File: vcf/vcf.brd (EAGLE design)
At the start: 88.9 x 107.6 mm, 102 parts, among them IC1 OPA4130U, IC2 OPA4130U, IC3 OPA4130U, IC4 OPA4130U, IC5 OPA4130U, Q1 BC847ASMD, Q2 BC847ASMD, Q3 BC847ASMD, Q4 BC847ASMD, Q5 BC847ASMD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

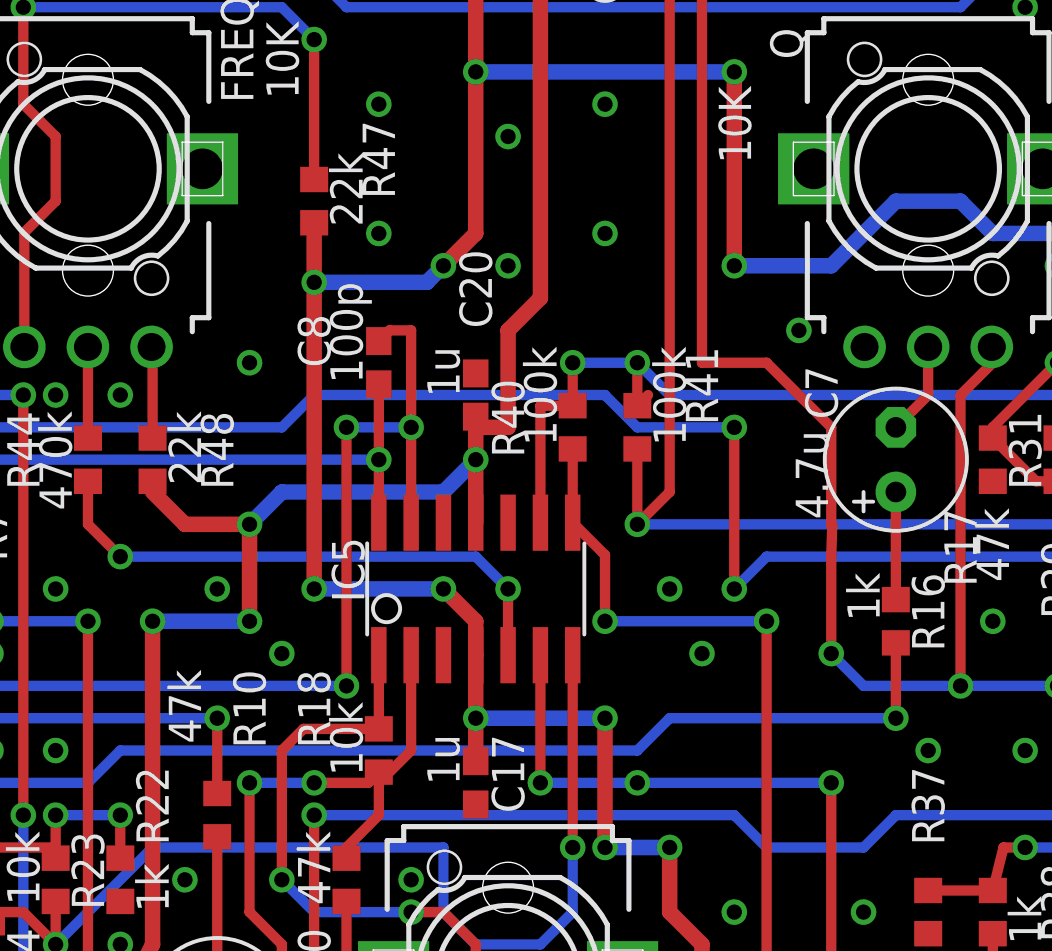
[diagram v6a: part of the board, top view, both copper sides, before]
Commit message: fixed bugs in vca.  did more changing of vcf components.  need to route a trace in vcf
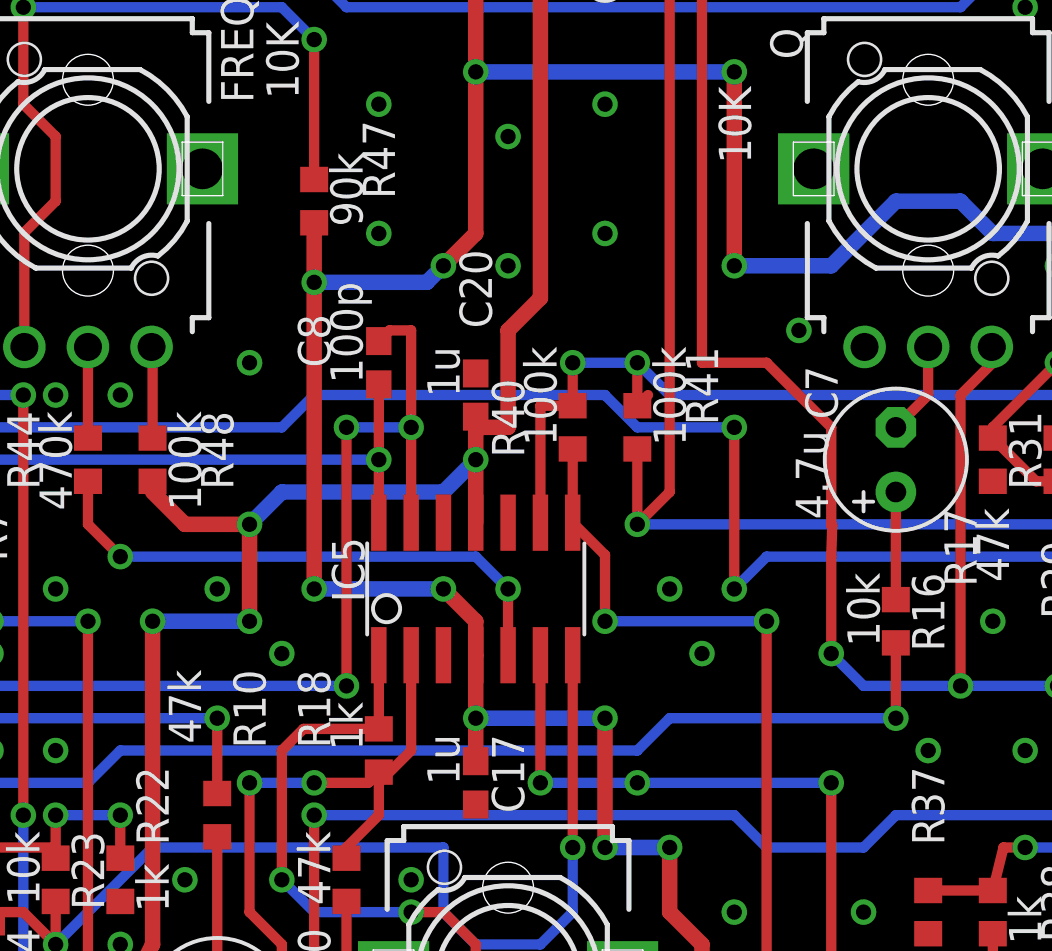
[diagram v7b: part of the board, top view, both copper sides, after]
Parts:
- R16: value 1k -> 10k
- R18: value 10k -> 1k
- R47: value 22k -> 90k
- R48: value 22k -> 100k
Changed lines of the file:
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@@
 <attribute name="VALUE" x="76.835" y="61.595" size="1.27" layer="21" font="vector" ratio="15" rot="R270"/>
 </element>
-<element name="R16" library="dan" package="R0603" value="1k" x="59.69" y="66.04" smashed="yes" rot="R90">
+<element name="R16" library="dan" package="R0603" value="10k" x="59.69" y="66.04" smashed="yes" rot="R90">
 <attribute name="NAME" x="60.325" y="67.945" size="1.27" layer="21" font="vector" ratio="15" rot="R270"/>
 <attribute name="VALUE" x="57.785" y="67.945" size="1.27" layer="21" font="vector" ratio="15" rot="R270"/>
@@
 <attribute name="VALUE" x="62.865" y="70.485" size="1.27" layer="21" font="vector" ratio="15" rot="R270"/>
 </element>
-<element name="R18" library="dan" package="R0603" value="10k" x="39.37" y="60.96" smashed="yes" rot="R90">
+<element name="R18" library="dan" package="R0603" value="1k" x="39.37" y="60.96" smashed="yes" rot="R90">
 <attribute name="NAME" x="36.195" y="64.135" size="1.27" layer="21" font="vector" ratio="15" rot="R270"/>
 <attribute name="VALUE" x="37.465" y="62.865" size="1.27" layer="21" font="vector" ratio="15" rot="R270"/>
@@
 <attribute name="VALUE" x="83.185" y="17.145" size="1.27" layer="21" font="vector" ratio="15" rot="R270"/>
 </element>
-<element name="R47" library="dan" package="R0603" value="22k" x="36.83" y="82.55" smashed="yes" rot="R270">
+<element name="R47" library="dan" package="R0603" value="90k" x="36.83" y="82.55" smashed="yes" rot="R270">
 <attribute name="NAME" x="38.735" y="85.725" size="1.27" layer="21" font="vector" ratio="15" rot="R270"/>
 <attribute name="VALUE" x="37.465" y="84.455" size="1.27" layer="21" font="vector" ratio="15" rot="R270"/>
 </element>
-<element name="R48" library="dan" package="R0603" value="22k" x="30.48" y="72.39" smashed="yes" rot="R90">
+<element name="R48" library="dan" package="R0603" value="100k" x="30.48" y="72.39" smashed="yes" rot="R90">
 <attribute name="NAME" x="32.385" y="74.295" size="1.27" layer="21" font="vector" ratio="15" rot="R270"/>
 <attribute name="VALUE" x="31.115" y="74.295" size="1.27" layer="21" font="vector" ratio="15" rot="R270"/>
